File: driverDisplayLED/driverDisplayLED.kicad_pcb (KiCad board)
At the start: 2 copper layers, 59 parts, among them J1 Conn_01x12_Male, J10 Conn_01x12_Male, J11 Conn_01x12_Male, J12 Conn_01x12_Male, J13 Conn_01x12_Male, J14 Conn_01x12_Male, J15 Conn_01x12_Male, J16 Conn_01x12_Male, J17 Conn_01x12_Male, J2 Conn_01x12_Male, J3 Conn_01x12_Male, J4 Conn_02x08_Counter_Clockwise, J5 Conn_01x12_Male, J6 Conn_01x12_Male, J7 Conn_01x12_Male, J8 Conn_01x12_Male, J9 Conn_01x12_Male, Q1 FDS4953, Q2 FDS4953, Q3 FDS4953, Q4 FDS4953, Q5 FDS4953, Q6 FDS4953, Q7 FDS4953, Q8 FDS4953, U1 74HC245, U2 74HC595, U3 74HC595, U4 74HC245, U5 74HC138D, U6 74HC04, U7 74HC595, U8 74HC595, U9 74HC138D

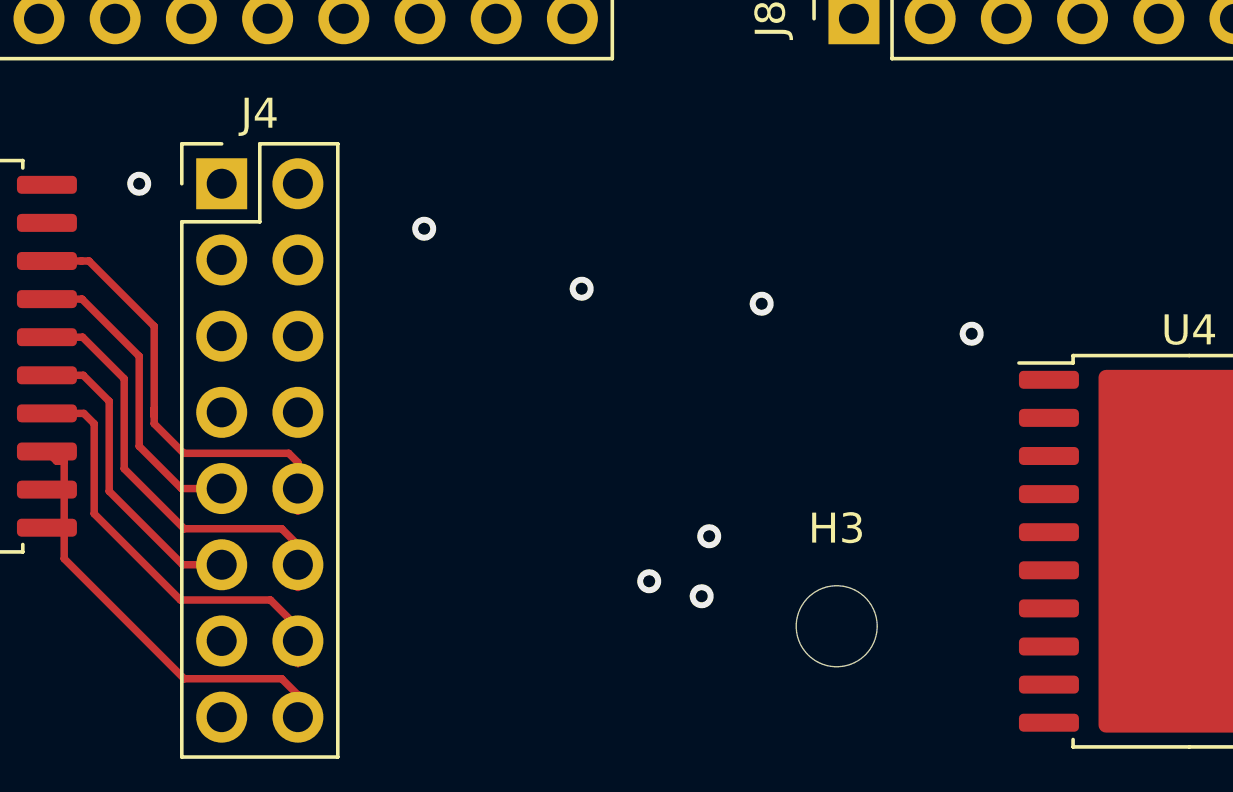
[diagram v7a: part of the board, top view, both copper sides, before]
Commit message: routing and mountholders
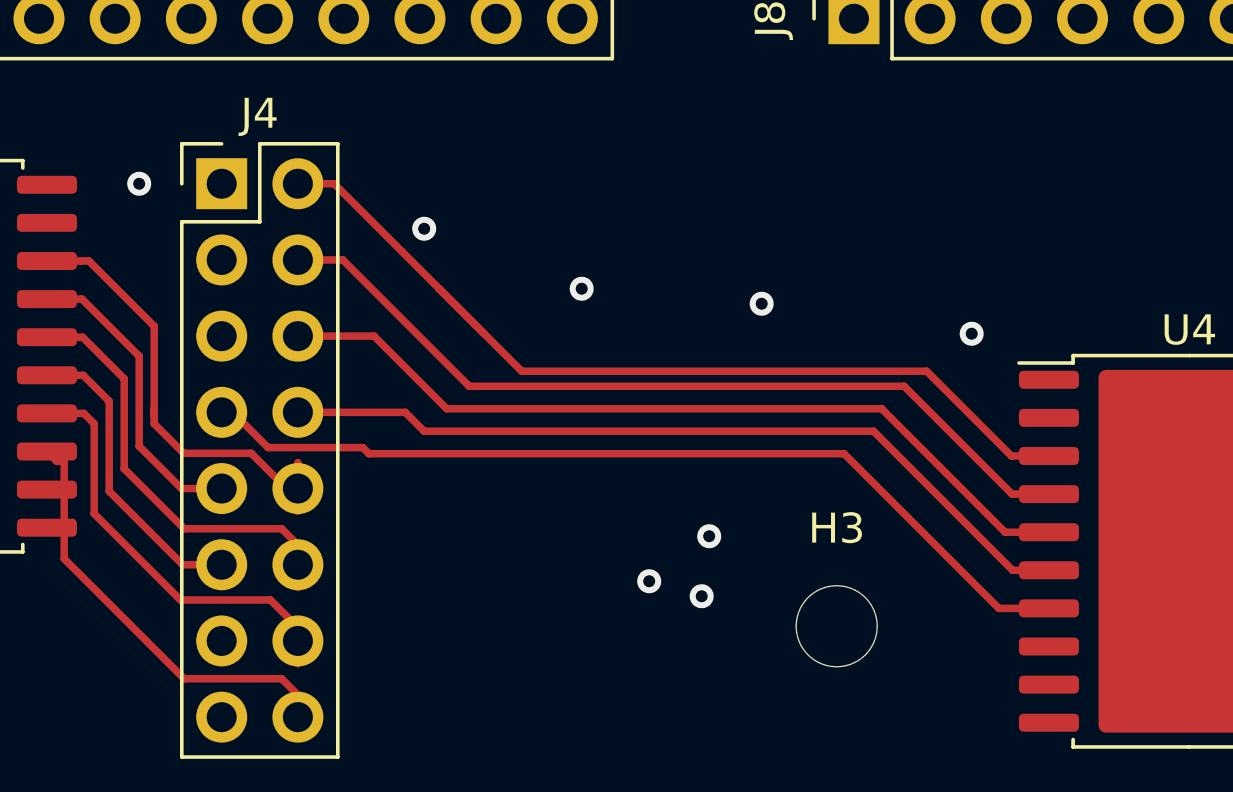
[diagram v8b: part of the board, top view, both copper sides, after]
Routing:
- net Net-(J4-Pad2): track 0.00 -> 30.9 mm
- net /a4-A5: track 0.00 -> 30.3 mm
- net Net-(J4-Pad4): track 0.00 -> 28.3 mm
- net Net-(J4-Pad6): track 0.00 -> 27.7 mm
- net Net-(J4-Pad8): track 0.00 -> 27.2 mm
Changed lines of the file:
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@@
     (thickness 1.6)
     (drawings 108)
-    (tracks 91)
+    (tracks 122)
     (zones 0)
     (modules 59)
@@
   (segment (start 77 110.75) (end 77 113.5) (width 0.25) (layer F.Cu) (net 8))
   (segment (start 77 113.5) (end 77 113.75) (width 0.25) (layer F.Cu) (net 8))
-  (segment (start 77.984999 114.984999) (end 81.484999 114.984999) (width 0.25) (layer F.Cu) (net 8))
   (segment (start 77 114) (end 77.984999 114.984999) (width 0.25) (layer F.Cu) (net 8))
   (segment (start 81.79 115.29) (end 81.79 116.16) (width 0.25) (layer F.Cu) (net 8))
-  (segment (start 81.484999 114.984999) (end 81.79 115.29) (width 0.25) (layer F.Cu) (net 8))
+  (segment (start 77.984999 114.984999) (end 80.234999 114.984999) (width 0.25) (layer F.Cu) (net 8))
+  (segment (start 81.41 116.16) (end 81.79 116.16) (width 0.25) (layer F.Cu) (net 8))
+  (segment (start 80.234999 114.984999) (end 81.41 116.16) (width 0.25) (layer F.Cu) (net 8))
   (segment (start 73.425 109.845) (end 74.595 109.845) (width 0.25) (layer F.Cu) (net 9))
   (segment (start 79.25 116.16) (end 77.91 116.16) (width 0.25) (layer F.Cu) (net 9))
@@
   (segment (start 112.25 70.75) (end 102.75 70.75) (width 0.25) (layer F.Cu) (net 19))
   (segment (start 117.5 70.75) (end 112.25 70.75) (width 0.25) (layer F.Cu) (net 19))
+  (segment (start 79.62 113.62) (end 79.25 113.62) (width 0.25) (layer F.Cu) (net 21))
+  (segment (start 80.795001 114.795001) (end 79.62 113.62) (width 0.25) (layer F.Cu) (net 21))
+  (segment (start 83.954999 114.795001) (end 80.795001 114.795001) (width 0.25) (layer F.Cu) (net 21))
+  (segment (start 84.159998 115) (end 83.954999 114.795001) (width 0.25) (layer F.Cu) (net 21))
+  (segment (start 100 115) (end 84.159998 115) (width 0.25) (layer F.Cu) (net 21))
+  (segment (start 105.155 120.155) (end 100 115) (width 0.25) (layer F.Cu) (net 21))
+  (segment (start 106.825 120.155) (end 105.155 120.155) (width 0.25) (layer F.Cu) (net 21))
   (segment (start 109.595 74.655) (end 109.595 73.5375) (width 0.25) (layer F.Cu) (net 140))
   (segment (start 109 75.25) (end 109.595 74.655) (width 0.25) (layer F.Cu) (net 140))
@@
   (segment (start 104.25 76.75) (end 105.75 75.25) (width 0.25) (layer F.Cu) (net 140))
   (segment (start 80.445 73.5375) (end 80.445 72.305) (width 0.25) (layer F.Cu) (net 140))
+  (segment (start 106.825 118.885) (end 105.615 118.885) (width 0.25) (layer F.Cu) (net 141))
+  (segment (start 105.615 118.885) (end 100.98 114.25) (width 0.25) (layer F.Cu) (net 141))
+  (segment (start 100.98 114.25) (end 86 114.25) (width 0.25) (layer F.Cu) (net 141))
+  (segment (start 85.37 113.62) (end 81.79 113.62) (width 0.25) (layer F.Cu) (net 141))
+  (segment (start 86 114.25) (end 85.37 113.62) (width 0.25) (layer F.Cu) (net 141))
+  (segment (start 81.79 111.08) (end 84.33 111.08) (width 0.25) (layer F.Cu) (net 142))
+  (segment (start 84.33 111.08) (end 86.75 113.5) (width 0.25) (layer F.Cu) (net 142))
+  (segment (start 86.75 113.5) (end 101.25 113.5) (width 0.25) (layer F.Cu) (net 142))
+  (segment (start 105.365 117.615) (end 106.825 117.615) (width 0.25) (layer F.Cu) (net 142))
+  (segment (start 101.25 113.5) (end 105.365 117.615) (width 0.25) (layer F.Cu) (net 142))
+  (segment (start 87.5 112.75) (end 83.29 108.54) (width 0.25) (layer F.Cu) (net 143))
+  (segment (start 83.29 108.54) (end 81.79 108.54) (width 0.25) (layer F.Cu) (net 143))
+  (segment (start 105.595 116.345) (end 102 112.75) (width 0.25) (layer F.Cu) (net 143))
+  (segment (start 102 112.75) (end 87.5 112.75) (width 0.25) (layer F.Cu) (net 143))
+  (segment (start 106.825 116.345) (end 105.595 116.345) (width 0.25) (layer F.Cu) (net 143))
+  (segment (start 81.79 106) (end 83 106) (width 0.25) (layer F.Cu) (net 144))
+  (segment (start 83 106) (end 85.25 108.25) (width 0.25) (layer F.Cu) (net 144))
+  (segment (start 106.825 115.075) (end 105.575 115.075) (width 0.25) (layer F.Cu) (net 144))
+  (segment (start 105.575 115.075) (end 102.75 112.25) (width 0.25) (layer F.Cu) (net 144))
+  (segment (start 89.25 112.25) (end 86.5 109.5) (width 0.25) (layer F.Cu) (net 144))
+  (segment (start 102.75 112.25) (end 89.25 112.25) (width 0.25) (layer F.Cu) (net 144))
+  (segment (start 86.5 109.5) (end 88 111) (width 0.25) (layer F.Cu) (net 144))
+  (segment (start 85.25 108.25) (end 86.5 109.5) (width 0.25) (layer F.Cu) (net 144))
   (zone (net 1) (net_name GND) (layer F.Cu) (hatch edge 0.508)
     (connect_pads (clearance 0.8))
